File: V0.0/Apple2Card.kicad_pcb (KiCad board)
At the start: 2 copper layers, 213.5 x 79.1 mm, 62 parts, among them J1 Conn_01x08_Pin, P2 Conn_02x13_Top_Bottom, SW1 SW_DIP_x08, U1C1 74LS240, U1E1 74LS14, U2 74LS133, U2B1 74LS08, U2D1 74LS138, U2E1 74LS09, U3A1 2764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

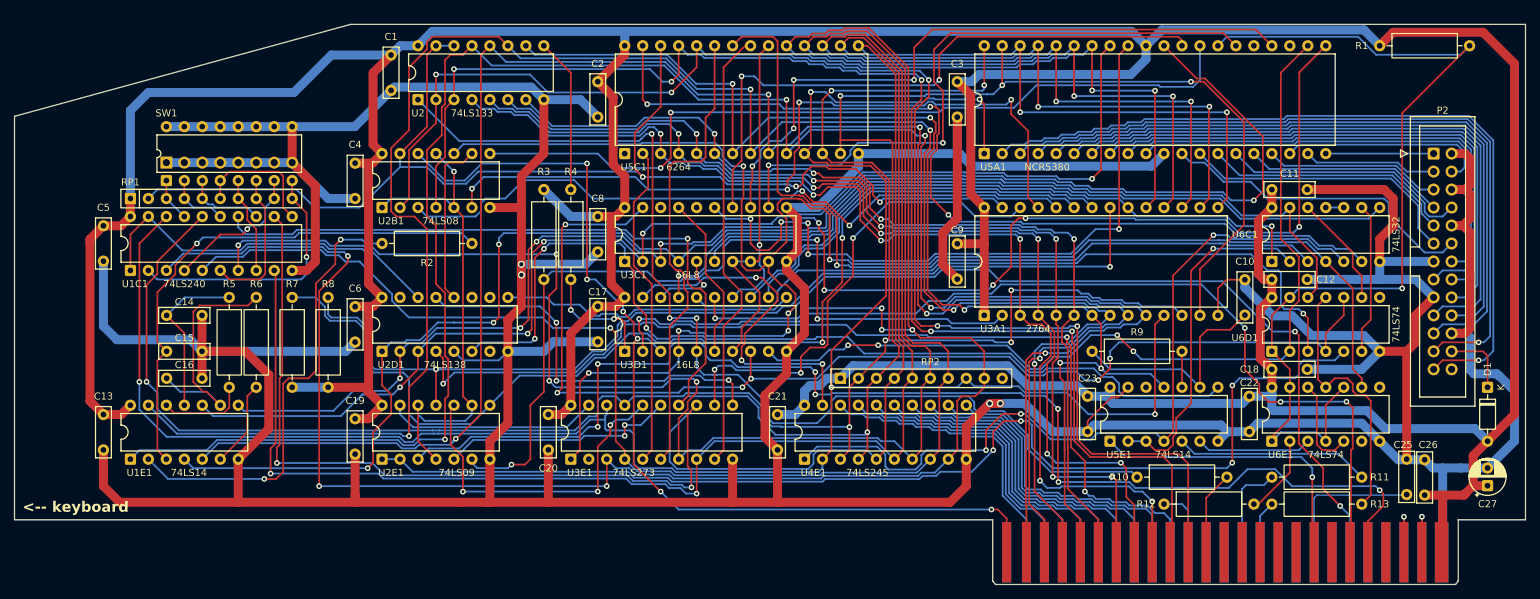
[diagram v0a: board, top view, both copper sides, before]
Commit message: directory organisation
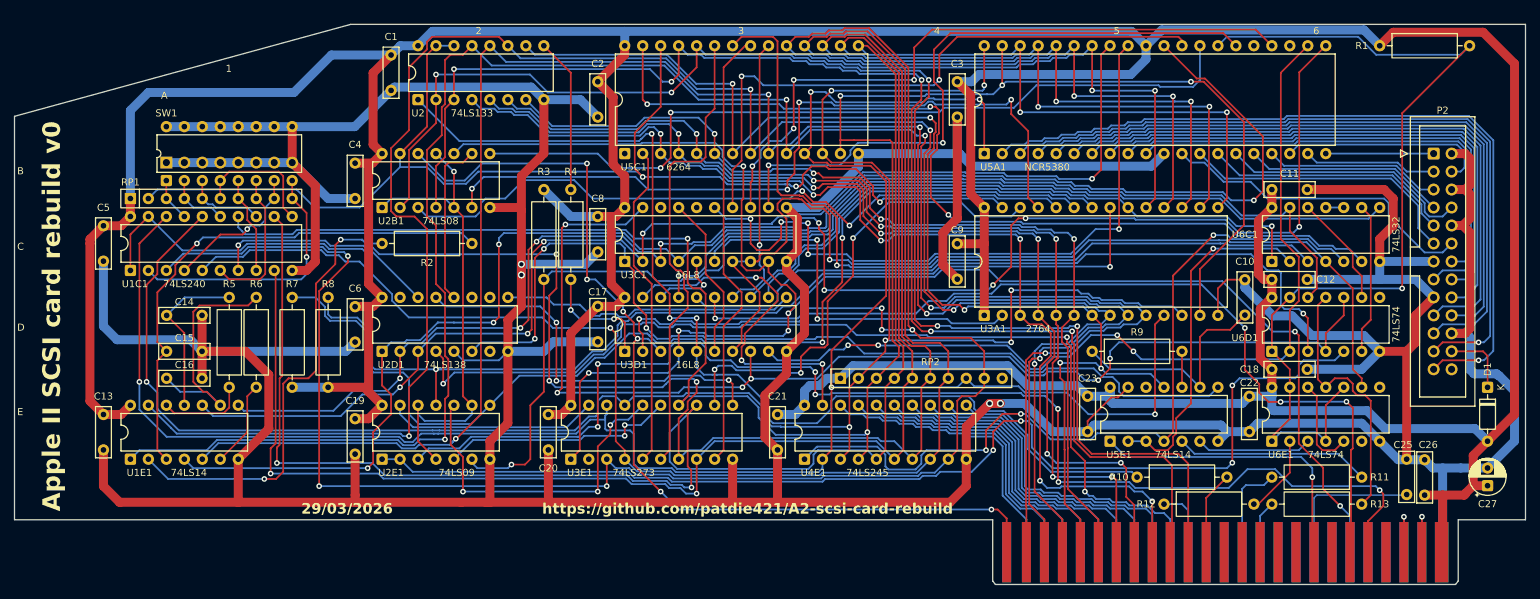
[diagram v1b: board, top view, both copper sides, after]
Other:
- board text added: "1"
- board text added: "2"
- board text added: "29/03/2026"
- board text added: "3"
- board text added: "4"
- board text added: "5"
- board text added: "6"
- board text added: "A"
- board text added: "Apple II SCSI card rebuild v0"
- board text added: "B"
- board text added: "C"
- board text added: "D"
- board text added: "E"
- board text added: "https://github.com/patdie421/A2-scsi-card-rebuild"
- board text removed: "<-- keyboard"
